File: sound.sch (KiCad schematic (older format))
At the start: 13 parts, among them IC1 MAX4466EXK+T

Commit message: Now amplifier is in local lib, hopefully.
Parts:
- IC1: footprint SamacSys_Parts:SOT65P210X110-5N -> Special_Parts:SOT65P210X110-5N; symbol SamacSys_Parts:MAX4466EXK+T -> Special_Parts:MAX4466EXK+T
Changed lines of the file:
@@
 $EndDescr
 $Comp
-L SamacSys_Parts:MAX4466EXK+T IC?
+L Special_Parts:MAX4466EXK+T IC?
 U 1 1 60997FE9
 P 5250 2400
@@
 F 0 "IC1" H 5750 2665 50  0000 C CNN
 F 1 "MAX4466EXK+T" H 5750 2574 50  0000 C CNN
-F 2 "SamacSys_Parts:SOT65P210X110-5N" H 6100 2500 50  0001 L CNN
+F 2 "Special_Parts:SOT65P210X110-5N" H 6100 2500 50  0001 L CNN
 F 3 "https://datasheets.maximintegrated.com/en/ds/MAX4465-MAX4469.pdf" H 6100 2400 50  0001 L CNN
 F 4 "Microphone Preamplifiers uPower Microphone Preamplifier" H 6100 2300 50  0001 L CNN "Description"

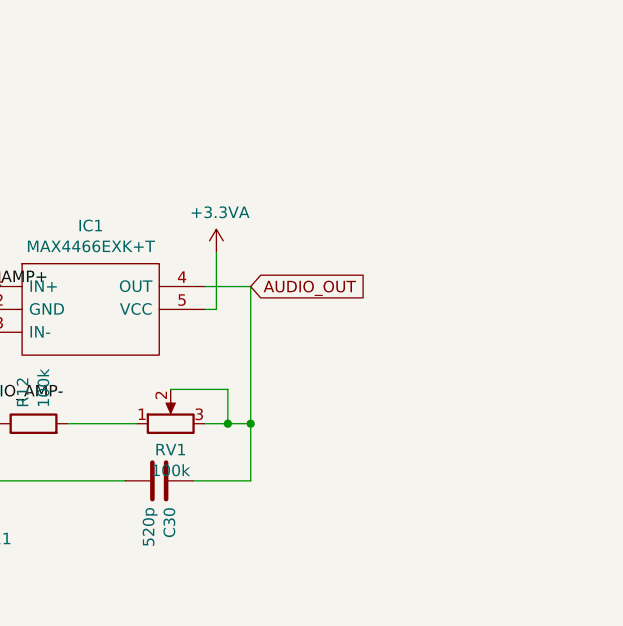
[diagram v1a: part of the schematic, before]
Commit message: Added some 1206 caps to be large stabilizing capacitors. Added a rank 1 RC filter to audio out, with a bypass solderbridge if wanted.
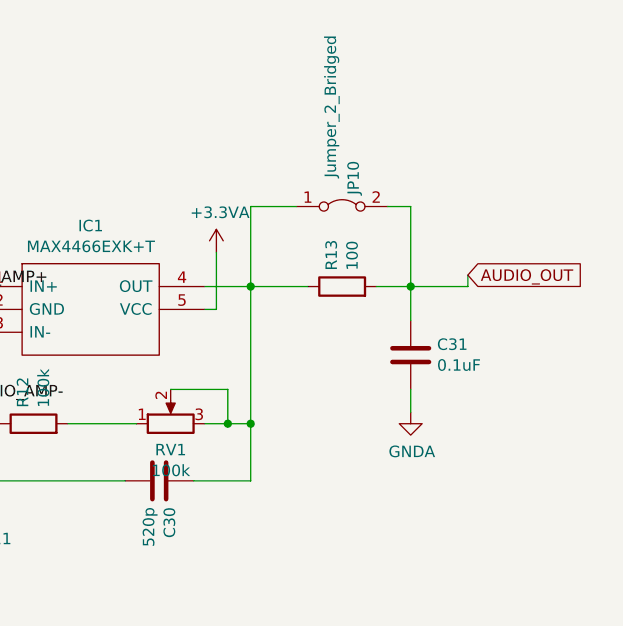
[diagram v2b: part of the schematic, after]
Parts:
- added C31: 0.1uF, Capacitor_SMD:C_0603_1608Metric, symbol Device:C
- added JP10: Jumper_2_Bridged, Jumper:SolderJumper-2_P1.3mm_Open_TrianglePad1.0x1.5mm, symbol Jumper:Jumper_2_Bridged
- added R13: 100, Resistor_SMD:R_0603_1608Metric_Pad0.98x0.95mm_HandSolder, symbol Device:R
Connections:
- net AUDIO_OUT: now also C31.1, JP10.2 (B), R13.2; no longer C30.1, IC1.4 (OUT), RV1.2, RV1.3
- net GNDA: now also C31.2
- new net: C30.1, IC1.4 (OUT), JP10.1 (A), R13.1, RV1.2, RV1.3
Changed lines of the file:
@@
 	6200 3250 6450 3250
-Wire Wire Line
-	6450 2400 6250 2400
 Wire Wire Line
 	6300 2250 6300 2500
 Wire Wire Line
 	6300 2500 6250 2500
-Text GLabel 6450 2400 2    50   Input ~ 0
+Text GLabel 7400 2350 2    50   Input ~ 0
 AUDIO_OUT
 $Comp
@@
 	5650 3000 5950 3000
 Wire Wire Line
-	6450 2400 6450 3000
-Wire Wire Line
 	6100 2850 6350 2850
 Wire Wire Line
@@
 	6350 3000 6450 3000
 Connection ~ 6350 3000
-Connection ~ 6450 3000
 Wire Wire Line
 	6450 3000 6450 3250
@@
 Text Label 5100 2400 0    50   ~ 0
 AUDIO_AMP+
+$Comp
+L Device:R R?
+U 1 1 61522A62
+P 6850 2400
+AR Path="/61522A62" Ref="R?"  Part="1"
+AR Path="/6099554C/61522A62" Ref="R13"  Part="1"
+F 0 "R13" H 6920 2446 50  0000 L CNN
+F 1 "100" H 6920 2355 50  0000 L CNN
+F 2 "Resistor_SMD:R_0603_1608Metric_Pad0.98x0.95mm_HandSolder" V 6780 2400 50  0001 C CNN
+F 3 "~" H 6850 2400 50  0001 C CNN
+	1    6850 2400
+	0    -1   -1   0
+$EndComp
+$Comp
+L Device:C C?
+U 1 1 615259FD
+P 7150 2700
+AR Path="/615259FD" Ref="C?"  Part="1"
+AR Path="/6099554C/615259FD" Ref="C31"  Part="1"
+F 0 "C31" H 7265 2746 50  0000 L CNN
+F 1 "0.1uF" H 7265 2655 50  0000 L CNN
+F 2 "Capacitor_SMD:C_0603_1608Metric" H 7188 2550 50  0001 C CNN
+F 3 "~" H 7150 2700 50  0001 C CNN
+	1    7150 2700
+	1    0    0    -1
+$EndComp
+Wire Wire Line
+	7000 2400 7150 2400
+Wire Wire Line
+	7150 2400 7150 2550
+Wire Wire Line
+	7150 2400 7400 2400
+Wire Wire Line
+	7400 2400 7400 2350
+Connection ~ 7150 2400
+Wire Wire Line
+	6250 2400 6450 2400
+Wire Wire Line
+	6450 2400 6450 3000
+Connection ~ 6450 3000
+$Comp
+L power:GNDA #PWR?
+U 1 1 6152A041
+P 7150 2950
+AR Path="/6152A041" Ref="#PWR?"  Part="1"
+AR Path="/6099554C/6152A041" Ref="#PWR0123"  Part="1"
+F 0 "#PWR0123" H 7150 2700 50  0001 C CNN
+F 1 "GNDA" H 7155 2777 50  0000 C CNN
+F 2 "" H 7150 2950 50  0001 C CNN
+F 3 "" H 7150 2950 50  0001 C CNN
+	1    7150 2950
+	1    0    0    -1
+$EndComp
+Wire Wire Line
+	7150 2950 7150 2850
+Wire Wire Line
+	6450 2400 6700 2400
+Connection ~ 6450 2400
+$Comp
+L Jumper:Jumper_2_Bridged JP?
+U 1 1 6153B171
+P 6850 2050
+AR Path="/6153B171" Ref="JP?"  Part="1"
+AR Path="/6099554C/6153B171" Ref="JP10"  Part="1"
+F 0 "JP10" V 6900 2250 50  0000 R CNN
+F 1 "Jumper_2_Bridged" V 6800 2800 50  0000 R CNN
+F 2 "Jumper:SolderJumper-2_P1.3mm_Open_TrianglePad1.0x1.5mm" H 6850 2050 50  0001 C CNN
+F 3 "~" H 6850 2050 50  0001 C CNN
+	1    6850 2050
+	1    0    0    -1
+$EndComp
+Wire Wire Line
+	6450 2400 6450 2050
+Wire Wire Line
+	6450 2050 6650 2050
+Wire Wire Line
+	7050 2050 7150 2050
+Wire Wire Line
+	7150 2050 7150 2400
 $EndSCHEMATC
